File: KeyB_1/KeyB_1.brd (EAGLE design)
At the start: 48 x 21 mm, 7 parts

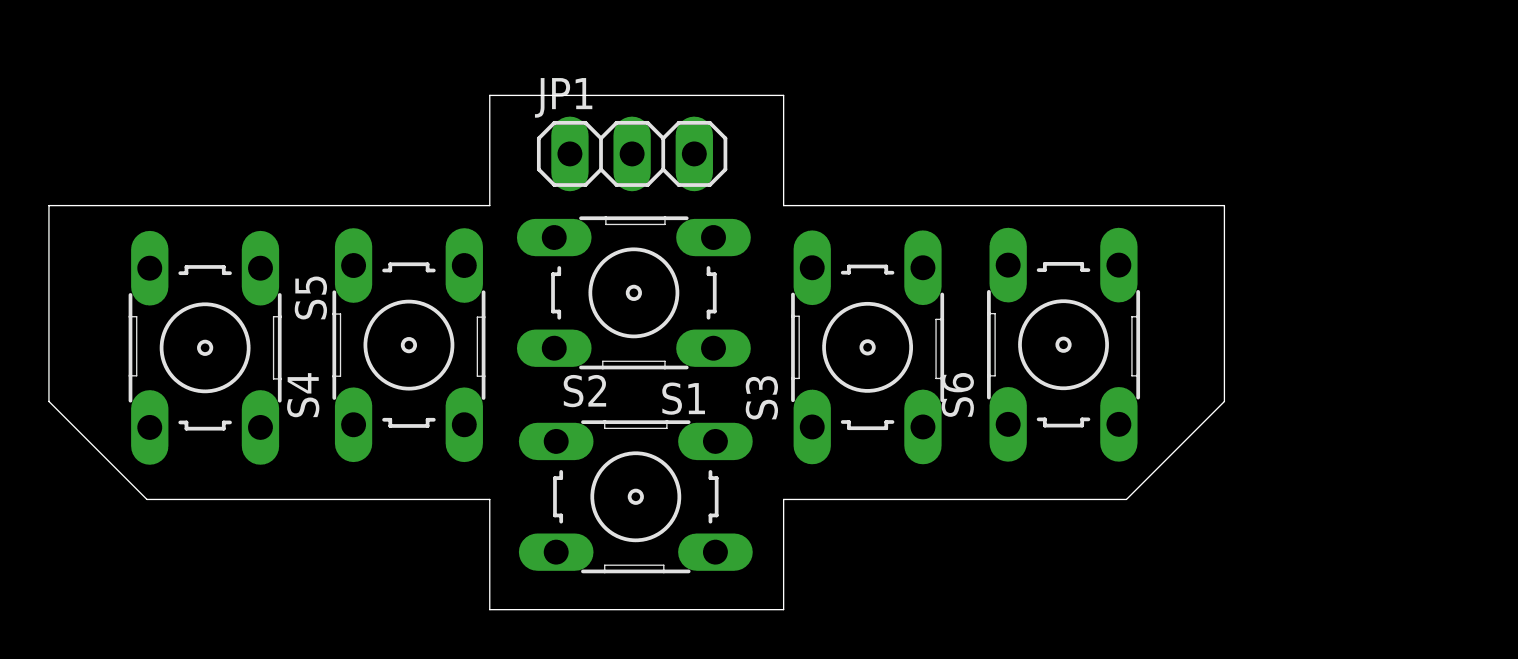
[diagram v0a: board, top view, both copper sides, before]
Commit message: changed keyboard schematic
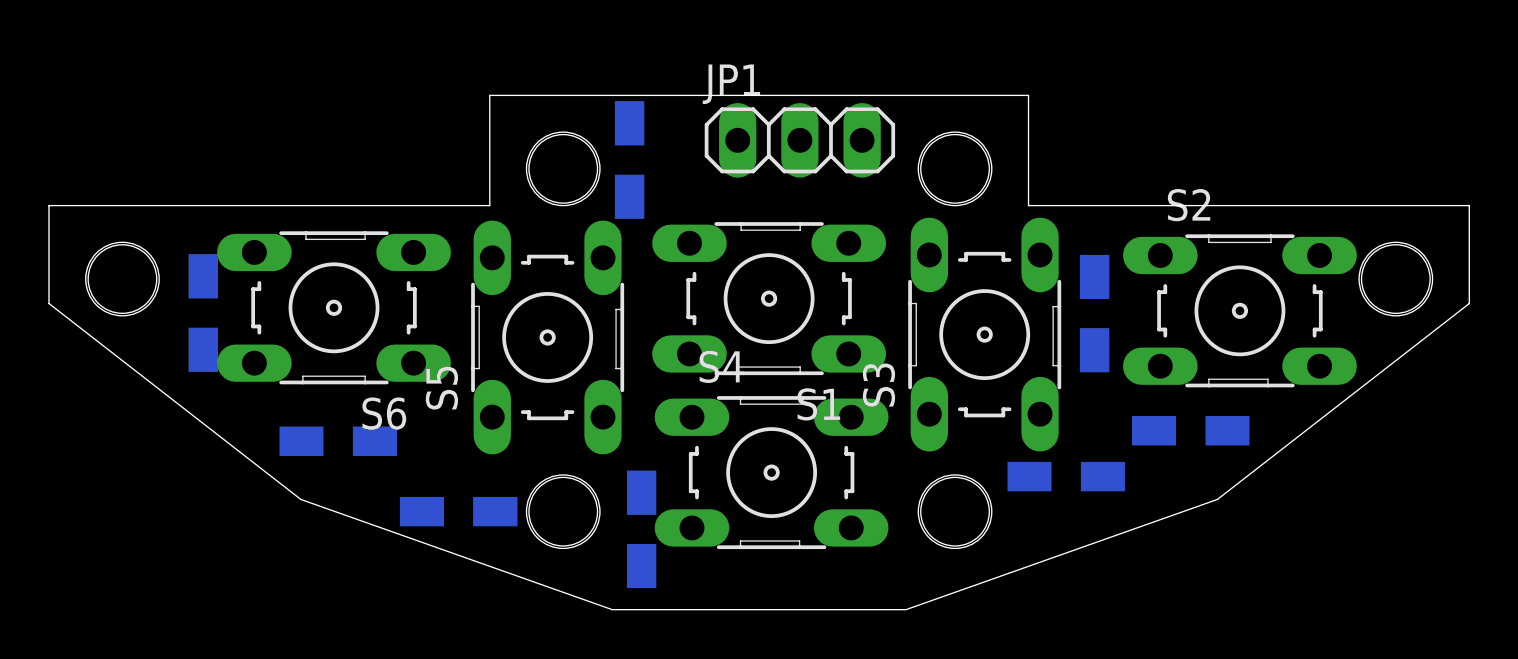
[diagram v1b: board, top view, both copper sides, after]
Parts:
- added R1, R2, R3, R4, R5, R7, R8: 1K, rcl:R1206W
- added R6: 1M, rcl:R1206W
- JP1: value (none) -> CON
- S1: value (none) -> BTN1
- S2: value (none) -> BTN2
- S3: value (none) -> BTN3
- S4: value (none) -> BTN4
- S5: value (none) -> BTN5
- S6: value (none) -> BTN6
- moved S6 29.8 mm to (11.6, 12.3), turned to 180 degrees
- moved S2 25.8 mm to (48.6, 12.2)
- moved S4 15.7 mm to (29.5, 5.60), turned to 0 degrees
- moved S5 14.0 mm to (20.4, 11.1), turned to 90 degrees
- moved JP1 6.87 mm to (30.7, 19.2)
- moved S1 5.53 mm to (29.4, 12.7)
- moved S3 4.81 mm to (38.2, 11.2)
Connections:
- new net +5V: JP1.1, R7.1
- new net AN_IN: JP1.3, R6.2, S1.3, S1.4, S2.3, S2.4, S3.3, S3.4, S4.3, S4.4, S5.3, S5.4, S6.3, S6.4
- new net GND: JP1.2, R6.1, R8.1
- new net N$1: R5.2, R7.2, S6.1, S6.2
- new net N$2: R4.2, R5.1, S5.1, S5.2
- new net N$3: R2.2, R3.1, S3.1, S3.2
- new net N$4: R3.2, R4.1, S4.1, S4.2
- new net N$5: R1.1, R8.2, S1.1, S1.2
- new net N$7: R1.2, R2.1, S2.1, S2.2
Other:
- board size 48 x 21 mm -> 58 x 21 mm

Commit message: finished layout
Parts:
- S1: value BTN1 -> UP
- S2: value BTN2 -> CANCEL
- S3: value BTN3 -> RIGHT
- S4: value BTN4 -> DOWN
- S5: value BTN5 -> LEFT
- S6: value BTN6 -> OK
- moved R1 0.50 mm to (46.6, 7.81)
- moved R2 0.50 mm to (41.5, 4.93)
- moved R4 0.50 mm to (16.7, 4.50)
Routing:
- net AN_IN: track 0.00 -> 82.5 mm
- net +5V: track 0.00 -> 29.2 mm
- net N$3: track 0.00 -> 28.4 mm
- net N$5: track 0.00 -> 28.0 mm
- net GND: track 0.00 -> 26.8 mm
- net N$7: track 0.00 -> 21.4 mm
- net N$4: track 0.00 -> 18.3 mm
- net N$2: track 0.00 -> 14.4 mm
- net N$1: track 0.00 -> 13.5 mm

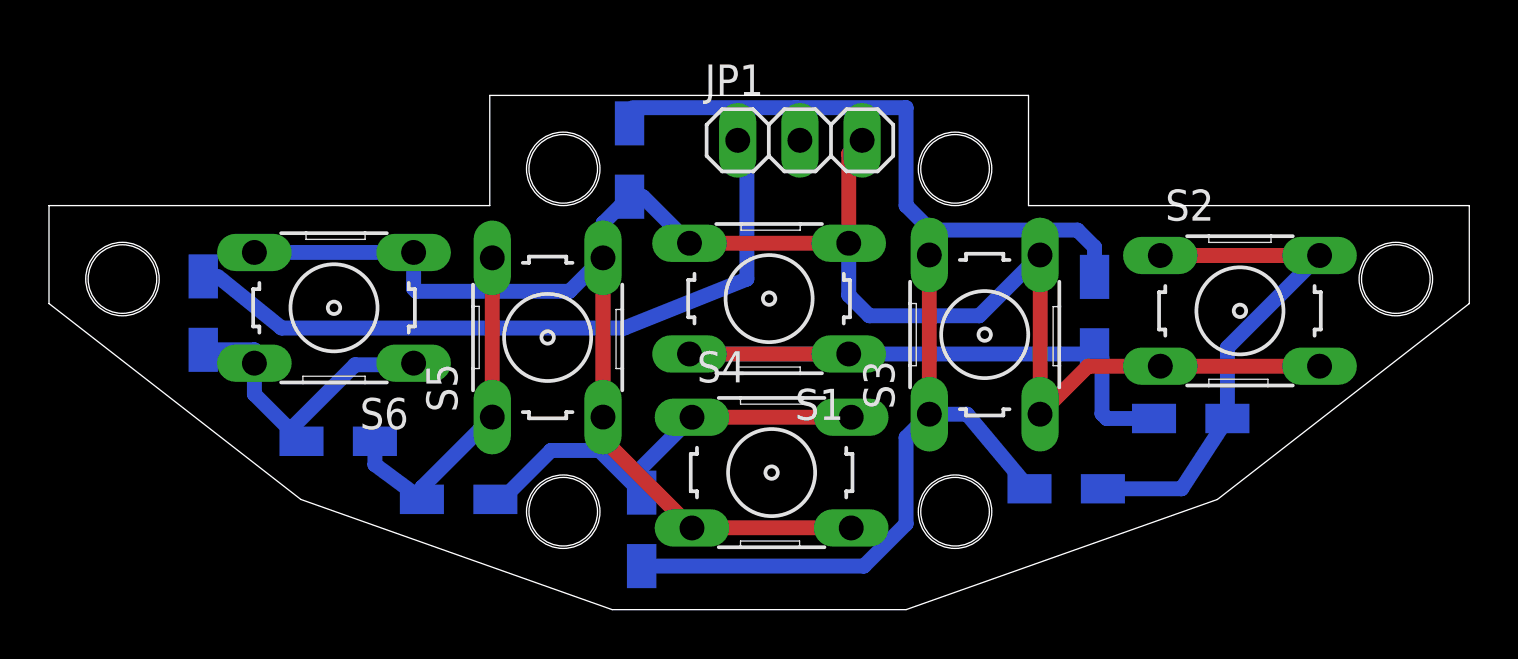
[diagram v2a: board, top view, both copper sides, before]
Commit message: corrected connect button
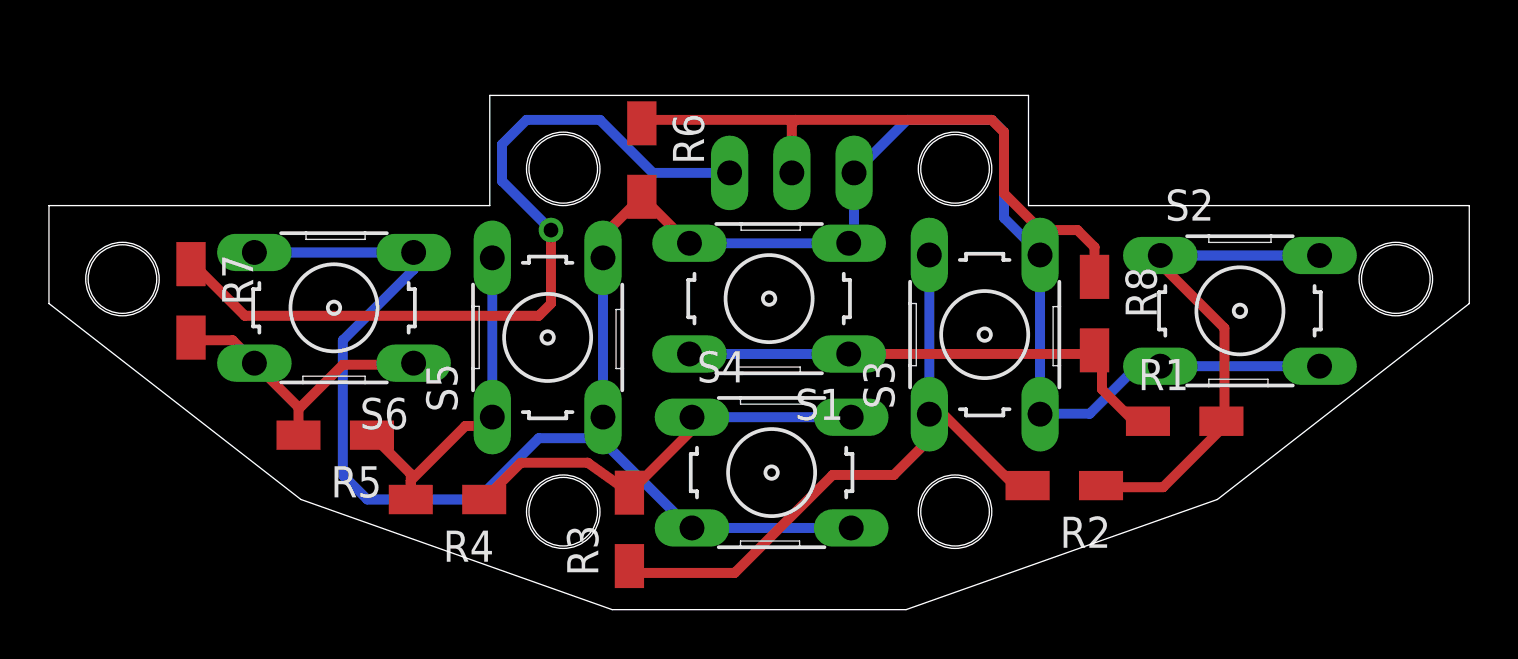
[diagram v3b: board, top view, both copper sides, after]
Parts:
- moved JP1 1.37 mm to (30.3, 17.8), flipped to the bottom, turned to 180 degrees
- moved R7 0.71 mm to (5.80, 12.6), flipped to the top
- moved R3 0.50 mm to (23.7, 3.28), flipped to the top
- moved R6 0.50 mm to (24.2, 18.4), flipped to the top
- moved R4 0.46 mm to (16.3, 4.50), flipped to the top, turned to 180 degrees
- moved R5 0.28 mm to (11.7, 7.12), flipped to the top, turned to 180 degrees
- moved R1 0.27 mm to (46.4, 7.69), flipped to the top, turned to 0 degrees
- moved R2 0.15 mm to (41.5, 5.07), flipped to the top, turned to 180 degrees
- flipped R8 to the top
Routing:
- net AN_IN: track 82.5 -> 94.9 mm
- net N$5: track 28.0 -> 21.0 mm
- net +5V: track 29.2 -> 33.7 mm
- net N$1: track 13.5 -> 12.2 mm
- net GND: track 26.8 -> 25.6 mm
- net N$3: track 28.4 -> 27.4 mm
- net N$4: track 18.3 -> 17.6 mm
- net N$7: track 21.4 -> 20.7 mm
- net N$2: track 14.4 -> 15.0 mm
